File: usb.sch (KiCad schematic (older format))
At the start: 8 parts, among them J5 USB_B_Micro, U10 USBLC6-2SC6

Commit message: Add digikey pn's to schematic, update BOM
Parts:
- C31: Digikey (none) -> 490-14466-1-ND
- C32: Digikey (none) -> 490-14603-1-ND
- J5: Digikey (none) -> 609-4050-1-ND; LCSC (none) -> C428495
- L5: Digikey (none) -> 587-1932-1-ND
- L6: Digikey (none) -> 490-5137-1-ND
- R16, R17: Digikey (none) -> 311-1.50KLRCT-ND
- U10: Digikey (none) -> 497-5235-1-ND
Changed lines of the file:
@@
 F 3 "~" H 3500 3500 50  0001 C CNN
 F 4 "C1015" V 3500 3500 50  0001 C CNN "LCSC"
+F 5 "587-1932-1-ND" V 3500 3500 50  0001 C CNN "Digikey"
 	1    3500 3500
 	0    -1   -1   0
@@
 F 3 "http://www2.st.com/resource/en/datasheet/CD00050750.pdf" H 6100 4100 50  0001 C CNN
 F 4 "C7519" V 5900 3750 50  0001 C CNN "LCSC"
+F 5 "497-5235-1-ND" V 5900 3750 50  0001 C CNN "Digikey"
 	1    5900 3750
 	0    1    1    0
@@
 F 3 "~" H 7150 3790 50  0001 C CNN
 F 4 "C86163" H 7150 3750 50  0001 C CNN "LCSC"
+F 5 "490-5137-1-ND" H 7150 3750 50  0001 C CNN "Digikey"
 	1    7150 3750
 	1    0    0    1
@@
 F 3 "~" H 6450 4050 50  0001 C CNN
 F 4 "C1525" H 6450 4050 50  0001 C CNN "LCSC"
+F 5 "490-14603-1-ND" H 6450 4050 50  0001 C CNN "Digikey"
 	1    6450 4050
 	1    0    0    -1
@@
 F 3 "~" H 7950 3300 50  0001 C CNN
 F 4 "C25867" H 7950 3300 50  0001 C CNN "LCSC"
+F 5 "311-1.50KLRCT-ND" H 7950 3300 50  0001 C CNN "Digikey"
 	1    7950 3300
 	1    0    0    -1
@@
 F 3 "~" H 4200 4000 50  0001 C CNN
 F 4 "C1779" H 4200 4000 50  0001 C CNN "LCSC"
+F 5 "490-14466-1-ND" H 4200 4000 50  0001 C CNN "Digikey"
 	1    4200 4000
 	1    0    0    -1
@@
 F 3 "~" H 8250 3300 50  0001 C CNN
 F 4 "C25867" H 8250 3300 50  0001 C CNN "LCSC"
+F 5 "311-1.50KLRCT-ND" H 8250 3300 50  0001 C CNN "Digikey"
 	1    8250 3300
 	1    0    0    -1
@@
 F 2 "Connector_USB:USB_Micro-B_Amphenol_10103594-0001LF_Horizontal" H 2600 3650 50  0001 C CNN
 F 3 "~" H 2600 3650 50  0001 C CNN
-F 4 "" H 2450 3700 50  0001 C CNN "LCSC"
+F 4 "C428495" H 2450 3700 50  0001 C CNN "LCSC"
+F 5 "609-4050-1-ND" H 2450 3700 50  0001 C CNN "Digikey"
 	1    2450 3700
 	1    0    0    -1
@@
 	5150 3800 5150 2750
 $Comp
-L Graphic:Logo_Open_Hardware_Small #LOGO?
+L Graphic:Logo_Open_Hardware_Small #LOGO7
 U 1 1 5DD3F249
 P 10800 6850
-F 0 "#LOGO?" H 10800 7125 50  0001 C CNN
+F 0 "#LOGO7" H 10800 7125 50  0001 C CNN
 F 1 "Logo_Open_Hardware_Small" H 10800 6625 50  0001 C CNN
 F 2 "" H 10800 6850 50  0001 C CNN
@@
 $EndComp
 $Comp
-L Graphic:SYM_Radio_Waves_Large #SYM?
+L Graphic:SYM_Radio_Waves_Large #SYM7
 U 1 1 5DD3F24F
 P 10250 6800
-F 0 "#SYM?" H 10250 7000 50  0001 C CNN
+F 0 "#SYM7" H 10250 7000 50  0001 C CNN
 F 1 "SYM_Radio_Waves_Large" H 10250 6550 50  0001 C CNN
 F 2 "" H 10250 6600 50  0001 C CNN

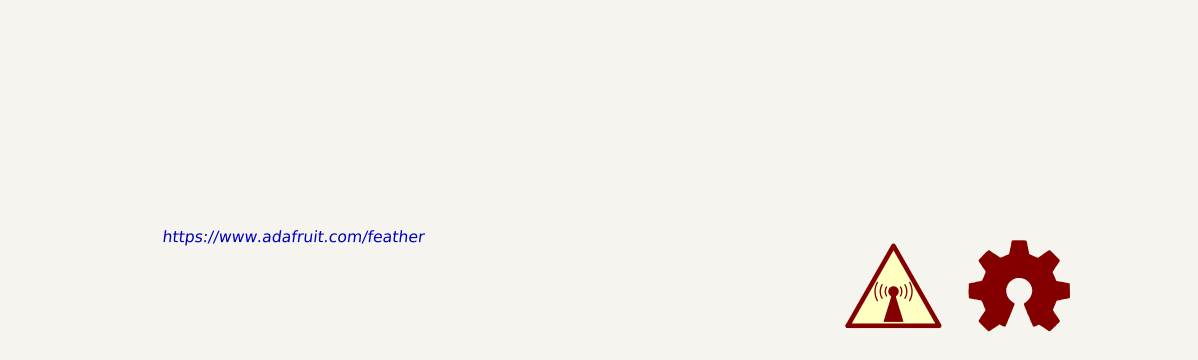
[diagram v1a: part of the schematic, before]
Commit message: PCB REV C0 * Make U8 footprint capable of crypto and fram device * Minor updates to schematic * Minor updates to doc prints * Update bot silk to REV C0
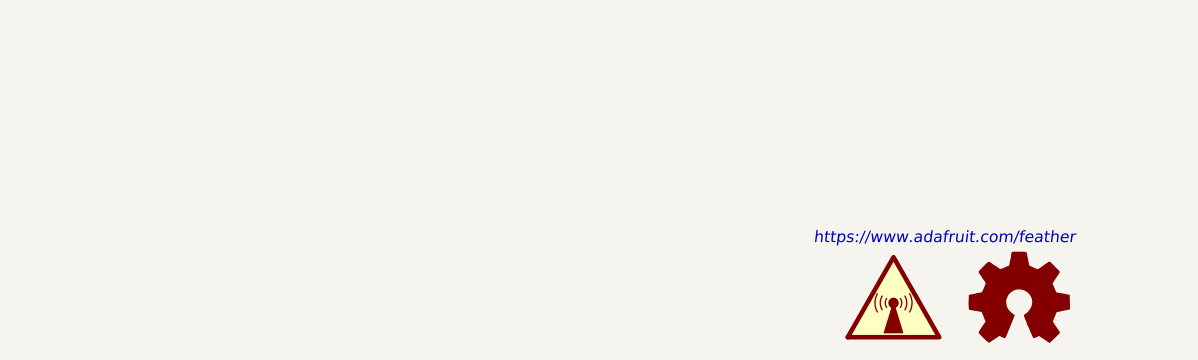
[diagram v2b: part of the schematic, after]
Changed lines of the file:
@@
 L Graphic:Logo_Open_Hardware_Small #LOGO7
 U 1 1 5DD3F249
-P 10800 6850
-F 0 "#LOGO7" H 10800 7125 50  0001 C CNN
-F 1 "Logo_Open_Hardware_Small" H 10800 6625 50  0001 C CNN
-F 2 "" H 10800 6850 50  0001 C CNN
-F 3 "~" H 10800 6850 50  0001 C CNN
-	1    10800 6850
+P 10800 6900
+F 0 "#LOGO7" H 10800 7175 50  0001 C CNN
+F 1 "Logo_Open_Hardware_Small" H 10800 6675 50  0001 C CNN
+F 2 "" H 10800 6900 50  0001 C CNN
+F 3 "~" H 10800 6900 50  0001 C CNN
+	1    10800 6900
 	1    0    0    -1
 $EndComp
@@
 L Graphic:SYM_Radio_Waves_Large #SYM7
 U 1 1 5DD3F24F
-P 10250 6800
-F 0 "#SYM7" H 10250 7000 50  0001 C CNN
-F 1 "SYM_Radio_Waves_Large" H 10250 6550 50  0001 C CNN
-F 2 "" H 10250 6600 50  0001 C CNN
-F 3 "~" H 10280 6600 50  0001 C CNN
-	1    10250 6800
+P 10250 6850
+F 0 "#SYM7" H 10250 7050 50  0001 C CNN
+F 1 "SYM_Radio_Waves_Large" H 10250 6600 50  0001 C CNN
+F 2 "" H 10250 6650 50  0001 C CNN
+F 3 "~" H 10280 6650 50  0001 C CNN
+	1    10250 6850
 	1    0    0    -1
 $EndComp
@@
 EndData
 $EndBitmap
-Text Notes 7050 6650 0    50   Italic 0
+Text Notes 9900 6650 0    50   Italic 0
 https://www.adafruit.com/feather
 $Bitmap
